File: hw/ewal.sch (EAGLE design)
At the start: 26 parts, among them U1 MMA8653FC, U2 ATTINY48

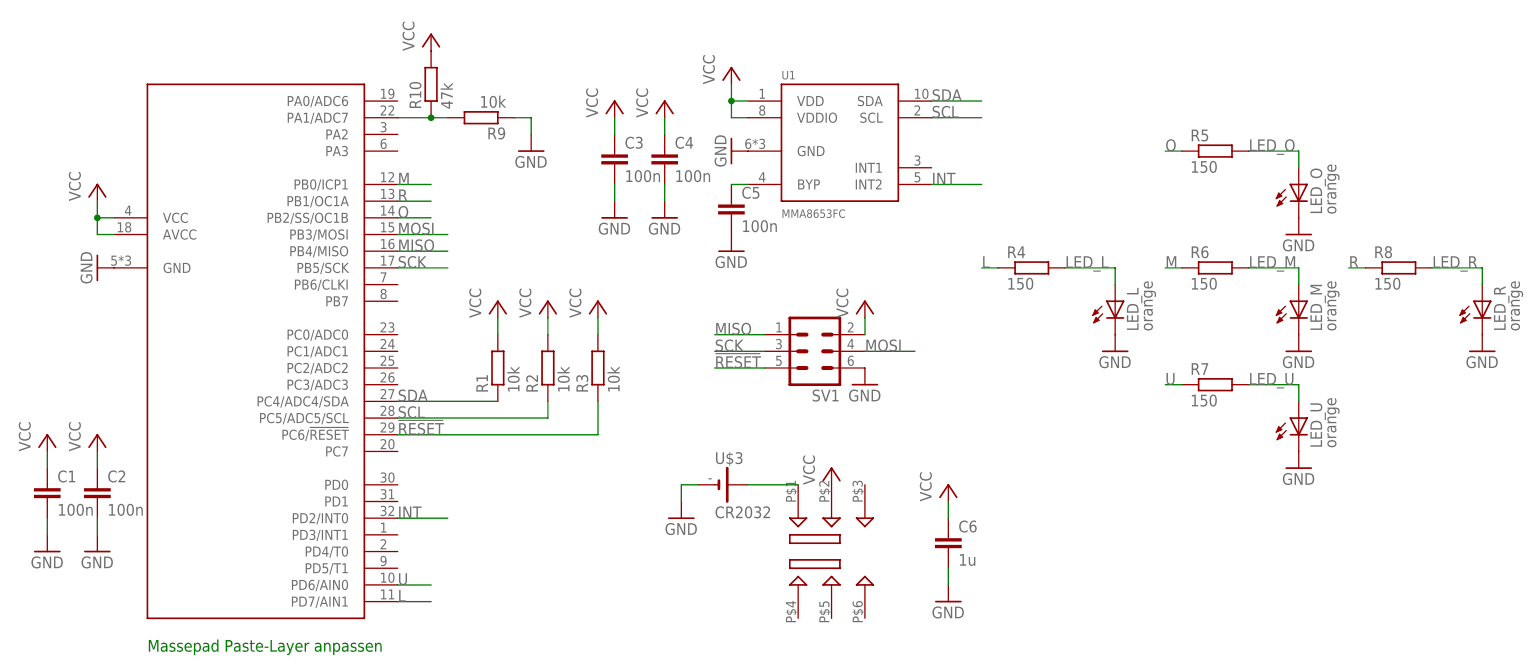
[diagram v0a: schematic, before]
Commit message: update to version 2
now with a touch sensor and a different stencil layout for the sensor
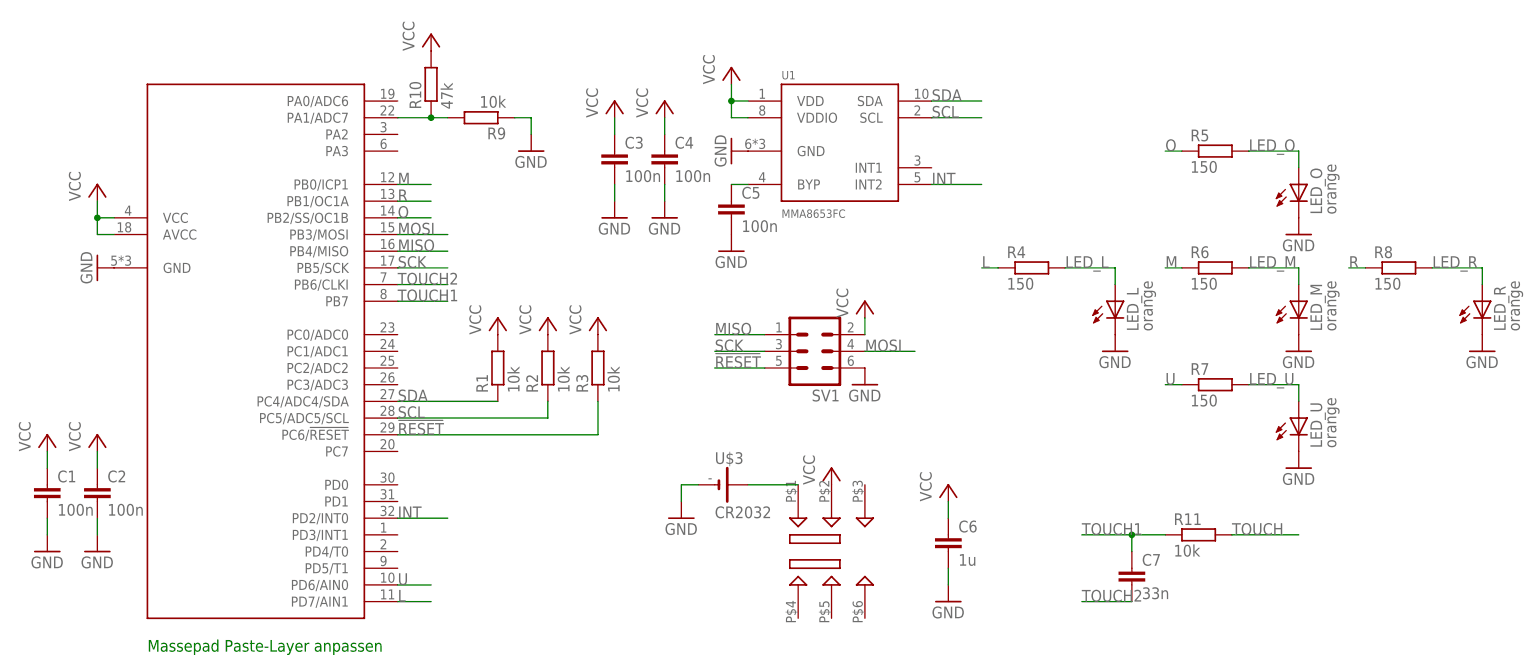
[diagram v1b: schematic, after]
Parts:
- added C7: 33n, rcl:C-EUC0603
- added R11: 10k, rcl:R-EU_R0603
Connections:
- new net TOUCH: R11.2
- new net TOUCH1: C7.1, R11.1, U2.PB7
- new net TOUCH2: C7.2, U2.PB6/CLKI
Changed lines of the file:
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@@
 <?xml version="1.0" encoding="utf-8"?>
 <!DOCTYPE eagle SYSTEM "eagle.dtd">
-<eagle version="6.4">
+<eagle version="7.1.0">
 <drawing>
 <settings>
@@
 <part name="GND16" library="supply1" deviceset="GND" device=""/>
 <part name="P+13" library="supply1" deviceset="VCC" device=""/>
+<part name="C7" library="rcl" deviceset="C-EU" device="C0603" value="33n"/>
+<part name="R11" library="rcl" deviceset="R-EU_" device="R0603" value="10k"/>
 </parts>
 <sheets>
@@
 <instance part="P+1" gate="VCC" x="10.16" y="66.04"/>
 <instance part="P+2" gate="VCC" x="106.68" y="83.82"/>
-<instance part="P+3" gate="VCC" x="71.12" y="48.26"/>
-<instance part="P+4" gate="VCC" x="78.74" y="48.26"/>
+<instance part="P+3" gate="VCC" x="71.12" y="45.72"/>
+<instance part="P+4" gate="VCC" x="78.74" y="45.72"/>
 <instance part="C1" gate="G$1" x="2.54" y="20.32"/>
 <instance part="C2" gate="G$1" x="10.16" y="20.32"/>
@@
 <instance part="GND7" gate="1" x="106.68" y="55.88"/>
 <instance part="R3" gate="G$1" x="86.36" y="38.1" rot="R90"/>
-<instance part="P+9" gate="VCC" x="86.36" y="48.26"/>
+<instance part="P+9" gate="VCC" x="86.36" y="45.72"/>
 <instance part="SV1" gate="1" x="119.38" y="40.64" rot="R180"/>
 <instance part="LED_L" gate="G$1" x="165.1" y="48.26"/>
@@
 <instance part="GND16" gate="1" x="76.2" y="71.12"/>
 <instance part="P+13" gate="VCC" x="60.96" y="88.9"/>
+<instance part="C7" gate="G$1" x="167.64" y="7.62"/>
+<instance part="R11" gate="G$1" x="177.8" y="12.7"/>
 </instances>
 <busses>
@@
 <pinref part="R1" gate="G$1" pin="2"/>
 <pinref part="P+3" gate="VCC" pin="VCC"/>
-<wire x1="71.12" y1="45.72" x2="71.12" y2="43.18" width="0.1524" layer="91"/>
 </segment>
 <segment>
 <pinref part="R2" gate="G$1" pin="2"/>
 <pinref part="P+4" gate="VCC" pin="VCC"/>
-<wire x1="78.74" y1="45.72" x2="78.74" y2="43.18" width="0.1524" layer="91"/>
 </segment>
 <segment>
 <pinref part="R3" gate="G$1" pin="2"/>
 <pinref part="P+9" gate="VCC" pin="VCC"/>
-<wire x1="86.36" y1="45.72" x2="86.36" y2="43.18" width="0.1524" layer="91"/>
 </segment>
 <segment>
@@
 </segment>
 </net>
+<net name="TOUCH2" class="0">
+<segment>
+<pinref part="U2" gate="G$1" pin="PB6/CLKI"/>
+<wire x1="55.88" y1="50.8" x2="63.5" y2="50.8" width="0.1524" layer="91"/>
+<label x="55.88" y="50.8" size="1.778" layer="95"/>
+</segment>
+<segment>
+<pinref part="C7" gate="G$1" pin="2"/>
+<wire x1="167.64" y1="2.54" x2="160.02" y2="2.54" width="0.1524" layer="91"/>
+<label x="160.02" y="2.54" size="1.778" layer="95"/>
+</segment>
+</net>
+<net name="TOUCH1" class="0">
+<segment>
+<pinref part="U2" gate="G$1" pin="PB7"/>
+<wire x1="55.88" y1="48.26" x2="63.5" y2="48.26" width="0.1524" layer="91"/>
+<label x="55.88" y="48.26" size="1.778" layer="95"/>
+</segment>
+<segment>
+<pinref part="R11" gate="G$1" pin="1"/>
+<pinref part="C7" gate="G$1" pin="1"/>
+<wire x1="172.72" y1="12.7" x2="167.64" y2="12.7" width="0.1524" layer="91"/>
+<wire x1="167.64" y1="12.7" x2="167.64" y2="10.16" width="0.1524" layer="91"/>
+<wire x1="167.64" y1="12.7" x2="160.02" y2="12.7" width="0.1524" layer="91"/>
+<junction x="167.64" y="12.7"/>
+<label x="160.02" y="12.7" size="1.778" layer="95"/>
+</segment>
+</net>
+<net name="TOUCH" class="0">
+<segment>
+<pinref part="R11" gate="G$1" pin="2"/>
+<wire x1="182.88" y1="12.7" x2="193.04" y2="12.7" width="0.1524" layer="91"/>
+<label x="182.88" y="12.7" size="1.778" layer="95"/>
+</segment>
+</net>
